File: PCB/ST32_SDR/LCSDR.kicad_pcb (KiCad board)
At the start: 2 copper layers, 150 x 95 mm, 121 parts, among them J1 MIC_PTT, J10 Conn_01x01, J11 Conn_01x01, J2 IDC10 Serial Wire, J3 Audio-Jack-3_2Switches, J4 LINEIN, J5 USB_B_Mini, J6 IQ, J7 CLK, J8 Conn_01x01, J9 Conn_01x01, K1 FRT5, K2 FRT5, Q1 Q_NPN_BEC, Q2 Q_NPN_BEC, Q7 BC817, SW1 SW_Push_Dual, SW2 SW_Push_Dual, SW3 SW_Push_Dual, SW4 SW_Push_Dual, SW5 ENCODER, SW6 SW_Push_Dual, U1 SI5351A, U15 Nokia_5110_LCD, U16 WM8731_alt, U2 FM24CL16B, U3 STM32F401RCTx, U4 AP1117-33, U5 MC34063, U6 MC34063, U7 78M09, Y1 20Mhz, Y2 Crystal

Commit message: PCB Windows 1
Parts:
- R25: moved to B.Cu
- moved R25 131.6 mm to (113.8, 66.0)
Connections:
- J2 pad 7: (no net) -> Net-(J2-Pad7)
- J2 pad 8: (no net) -> Net-(J2-Pad8)
- J3 pad 4: (no net) -> Net-(J3-Pad4)
- J3 pad 5: (no net) -> Net-(J3-Pad5)
- J5 pad 1: (no net) -> Net-(J5-Pad1)
- J5 pad 4: (no net) -> Net-(J5-Pad4)
- J6 pad 3: (no net) -> Net-(J6-Pad3)
- J6 pad 4: (no net) -> Net-(J6-Pad4)
- J6 pad 5: (no net) -> Net-(J6-Pad5)
- J6 pad 6: (no net) -> Net-(J6-Pad6)
- K2 pad 2: (no net) -> Net-(K2-Pad2)
- K2 pad 4: (no net) -> Q_OUT
- K2 pad 7: (no net) -> I_OUT
- R5 pad 2: (no net) -> TX2
- RN3 pad 5: (no net) -> Net-(RN3-Pad5)
- RN3 pad 6: (no net) -> Net-(RN3-Pad6)
- RN3 pad 7: (no net) -> Net-(RN3-Pad7)
- RN3 pad 8: (no net) -> Net-(RN3-Pad8)
- U16 pad 12: (no net) -> LINE_OUT_LEFT
- U16 pad 2: (no net) -> Net-(U16-Pad2)
- U16 pad 26: (no net) -> Net-(U16-Pad26)
- U2 pad 1: (no net) -> Net-(U2-Pad1)
- U2 pad 2: (no net) -> Net-(U2-Pad2)
- U2 pad 3: (no net) -> Net-(U2-Pad3)
- U3 pad 1: (no net) -> Net-(U3-Pad1)
- U3 pad 10: (no net) -> Net-(U3-Pad10)
- U3 pad 11: (no net) -> Net-(U3-Pad11)
- U3 pad 13: (no net) -> Net-(U3-Pad13)
- U3 pad 14: ENCODER_A -> Net-(U3-Pad14)
- U3 pad 15: ENCODER_B -> Net-(U3-Pad15)
- U3 pad 16: (no net) -> Net-(U3-Pad16)
- U3 pad 17: (no net) -> Net-(U3-Pad17)
- U3 pad 20: (no net) -> Net-(U3-Pad20)
- U3 pad 21: (no net) -> Net-(U3-Pad21)
- U3 pad 22: (no net) -> ENCODER_A
- U3 pad 23: (no net) -> ENCODER_B
- U3 pad 24: LCD_RESET -> Net-(U3-Pad24)
- U3 pad 25: LCD_LIGHT -> Net-(U3-Pad25)
- U3 pad 38: (no net) -> Net-(U3-Pad38)
- U3 pad 39: (no net) -> Net-(U3-Pad39)
- U3 pad 40: KEY_MENU -> I2C_SDA_MCU
- U3 pad 41: TX1 -> I2C_SCL_MCU
- U3 pad 42: (no net) -> Net-(U3-Pad42)
- U3 pad 43: (no net) -> Net-(U3-Pad43)
- U3 pad 54: (no net) -> LCD_RESET
- U3 pad 56: (no net) -> LCD_LIGHT
- U3 pad 57: (no net) -> I_IN_M2
- U3 pad 58: (no net) -> Q_IN_M1
- U3 pad 59: (no net) -> Q_IN_M2
- U3 pad 61: I2C_SCL_MCU -> Net-(U3-Pad61)
- U3 pad 62: I2C_SDA_MCU -> Net-(U3-Pad62)
- U3 pad 8: (no net) -> Net-(U3-Pad8)
- U3 pad 9: (no net) -> Net-(U3-Pad9)
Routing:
- net SWDIO: track 35.7 -> 44.5 mm, vias 2 -> 3
- net I2C_SCL_MCU: track 0.00 -> 8.40 mm
- net +3V3: track 18.8 -> 27.1 mm
- net Net-(R8-Pad1): track 0.00 -> 7.40 mm
- net I2C_SDA_MCU: track 0.00 -> 6.31 mm
- net ENCODER_A: track 0.00 -> 4.20 mm
- net ENCODER_B: track 0.00 -> 3.40 mm

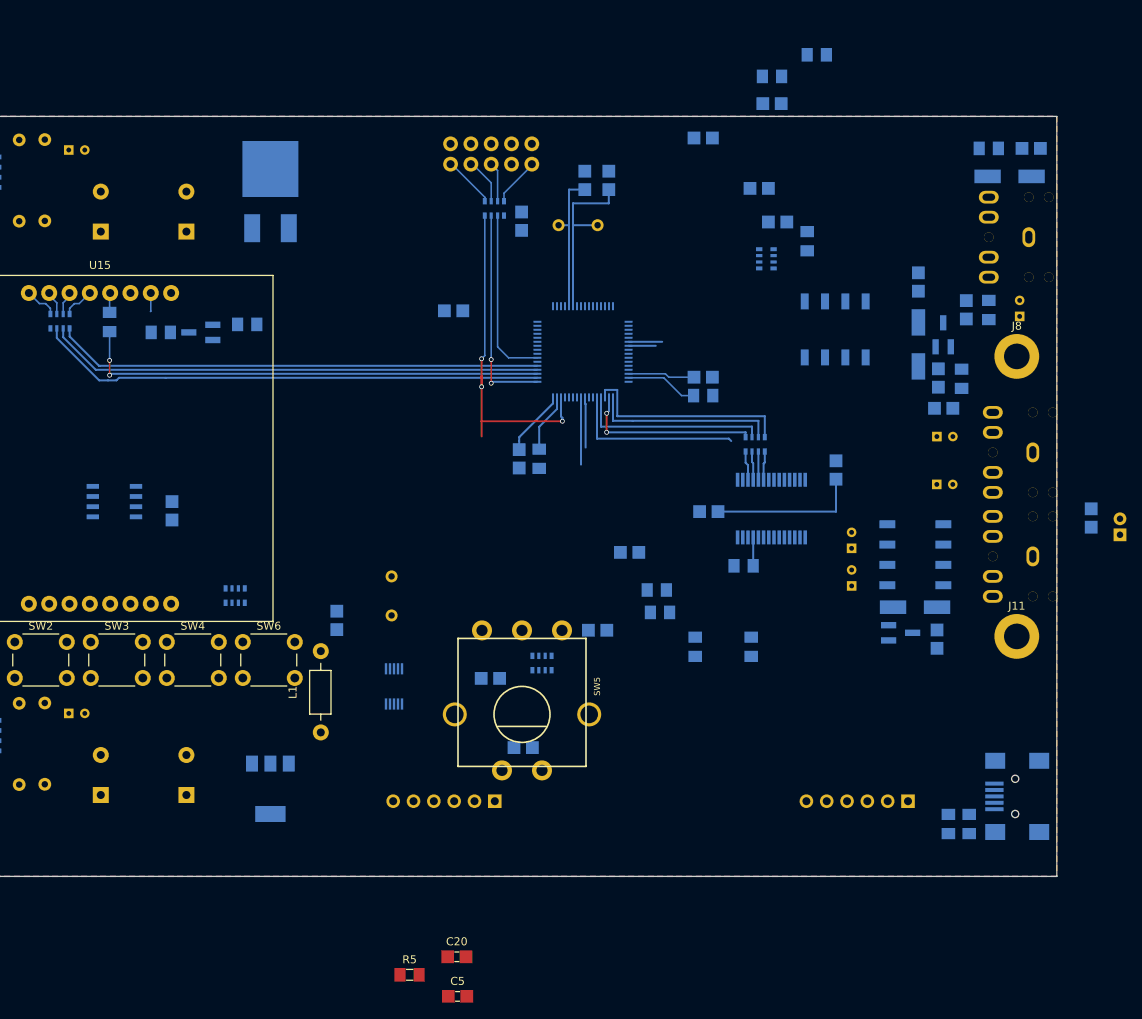
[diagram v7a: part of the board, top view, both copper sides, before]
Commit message: PCB Linux 2, update AUDIO_OUT
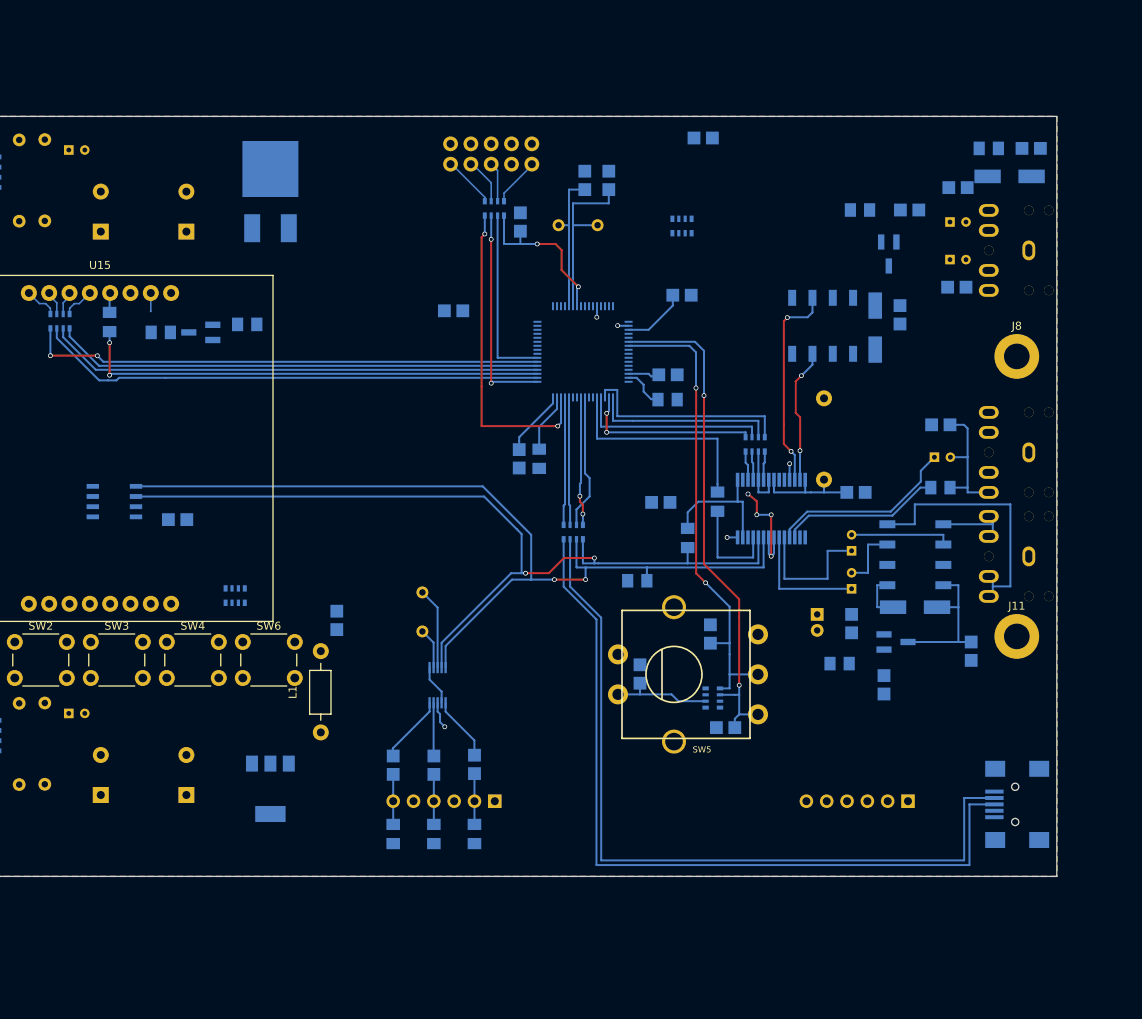
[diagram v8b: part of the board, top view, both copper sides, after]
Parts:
- removed J5: USB_B_Mini, Connect:USB_Mini-B
- removed R17, R18: 33, UI:R_1206_0603
- removed R22, R23: 56, UI:R_1206_0603
- added J12: USB_B_Mini, Connect:USB_Mini-B, B.Cu at (210.0, 126.0)
- added L4: 100uH, Choke_Axial_ThroughHole:Choke_Horizontal_RM10mm, B.Cu at (185.9, 80.4)
- added RN4: 47, Resistors_SMD:R_Array_Convex_4x0603, B.Cu at (154.6, 92.0)
- C20, C5, R5: moved to B.Cu
- moved R2 108.5 mm to (137.1, 129.7), turned to 270 degrees
- moved R3 105.9 mm to (132.1, 129.7), turned to 270 degrees
- moved C20 104.5 mm to (202.5, 61.4), turned to 180 degrees
- moved C4 95.3 mm to (132.1, 121.1), turned to 90 degrees
- moved R1 85.0 mm to (142.2, 129.7)
- moved C3 82.8 mm to (137.1, 121.1), turned to 90 degrees
- moved C2 77.7 mm to (142.2, 121.0), turned to 90 degrees
- moved R5 66.3 mm to (187.8, 108.4), turned to 180 degrees
- moved C5 66.0 mm to (193.4, 111.0), turned to 270 degrees
- moved C116 39.1 mm to (185.1, 102.2), turned to 270 degrees
- moved C33 32.8 mm to (168.2, 62.4)
- moved C44 32.7 mm to (189.3, 103.4), turned to 270 degrees
- moved C19 28.1 mm to (201.7, 57.9)
- moved C23 28.1 mm to (171.7, 104.7), turned to 90 degrees
- moved C18 27.6 mm to (202.7, 48.9)
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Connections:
- C2 pad 1: CLK0 -> CLK2
- C4 pad 1: CLK2 -> CLK0
- C45 pad 2: +3V3 -> Net-(C45-Pad2)
- J2 pad 7: Net-(J2-Pad7) -> (no net)
- J2 pad 8: Net-(J2-Pad8) -> (no net)
- J3 pad 4: Net-(J3-Pad4) -> (no net)
- J3 pad 5: Net-(J3-Pad5) -> (no net)
- J6 pad 3: Net-(J6-Pad3) -> (no net)
- J6 pad 4: Net-(J6-Pad4) -> (no net)
- J6 pad 5: Net-(J6-Pad5) -> (no net)
- J6 pad 6: Net-(J6-Pad6) -> (no net)
- J7 pad 2: CLK0 -> CLK2
- J7 pad 6: CLK2 -> CLK0
- K2 pad 2: Net-(K2-Pad2) -> (no net)
- K2 pad 4: Q_OUT -> (no net)
- K2 pad 7: I_OUT -> (no net)
- R1 pad 1: CLK0 -> CLK2
- R3 pad 1: CLK2 -> CLK0
- RN3 pad 5: Net-(RN3-Pad5) -> (no net)
- RN3 pad 6: Net-(RN3-Pad6) -> (no net)
- RN3 pad 7: Net-(RN3-Pad7) -> (no net)
- RN3 pad 8: Net-(RN3-Pad8) -> (no net)
- RN9 pad 1: KEY_MENU -> ENCODER_B
- RN9 pad 2: ENCODER_B -> ENCODER_A
- RN9 pad 3: ENCODER_A -> +3V3
- RN9 pad 4: KEY_E -> (no net)
- RN9 pad 5: +3V3 -> KEY_E
- RN9 pad 6: +3V3 -> KEY_MENU
- U1 pad 10: Net-(C2-Pad2) -> Net-(C4-Pad2)
- U1 pad 6: Net-(C4-Pad2) -> Net-(C2-Pad2)
- U16 pad 14: +3V3 -> Net-(C45-Pad2)
- U16 pad 2: Net-(U16-Pad2) -> (no net)
- U16 pad 26: Net-(U16-Pad26) -> (no net)
- U16 pad 8: +3V3 -> Net-(C45-Pad2)
- U2 pad 1: Net-(U2-Pad1) -> (no net)
- U2 pad 2: Net-(U2-Pad2) -> (no net)
- U2 pad 3: Net-(U2-Pad3) -> (no net)
- U3 pad 1: Net-(U3-Pad1) -> (no net)
- U3 pad 10: Net-(U3-Pad10) -> BAND2
- U3 pad 11: Net-(U3-Pad11) -> BAND3
- U3 pad 13: Net-(U3-Pad13) -> (no net)
- U3 pad 14: Net-(U3-Pad14) -> (no net)
- U3 pad 15: Net-(U3-Pad15) -> (no net)
- U3 pad 16: Net-(U3-Pad16) -> (no net)
- U3 pad 17: Net-(U3-Pad17) -> (no net)
- U3 pad 20: Net-(U3-Pad20) -> (no net)
- U3 pad 21: Net-(U3-Pad21) -> TX1
- U3 pad 24: Net-(U3-Pad24) -> (no net)
- U3 pad 25: Net-(U3-Pad25) -> (no net)
- U3 pad 26: BAND0 -> (no net)
- U3 pad 27: BAND1 -> (no net)
- U3 pad 28: BAND2 -> (no net)
- U3 pad 29: BAND3 -> (no net)
- U3 pad 38: Net-(U3-Pad38) -> (no net)
- U3 pad 39: Net-(U3-Pad39) -> TX2
- U3 pad 42: Net-(U3-Pad42) -> (no net)
- U3 pad 43: Net-(U3-Pad43) -> (no net)
- U3 pad 57: I_IN_M2 -> (no net)
- U3 pad 58: Q_IN_M1 -> (no net)
- U3 pad 59: Q_IN_M2 -> (no net)
- U3 pad 61: Net-(U3-Pad61) -> (no net)
- U3 pad 62: Net-(U3-Pad62) -> (no net)
- U3 pad 8: Net-(U3-Pad8) -> BAND0
- U3 pad 9: Net-(U3-Pad9) -> BAND1
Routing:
- net I2C_SDA: track 0.00 -> 115.0 mm, vias 0 -> 2
- net I2C_SCL: track 0.00 -> 112.5 mm, vias 0 -> 2
- net Net-(J12-Pad3): track 0.00 -> 99.7 mm
- net Net-(J12-Pad2): track 0.00 -> 98.7 mm
- net LCD_RESET: track 0.00 -> 64.6 mm, vias 0 -> 2
- net ENCODER_A: track 4.20 -> 63.8 mm, vias 0 -> 2
- net ENCODER_B: track 3.40 -> 59.7 mm, vias 0 -> 2
- net Net-(J4-Pad1): track 0.00 -> 32.8 mm
- net LINE_OUT_LEFT: track 0.00 -> 26.3 mm, vias 0 -> 2
- net GND: track 0.00 -> 24.6 mm, vias 0 -> 9
- net MIC_IN: track 0.00 -> 23.6 mm
- net MCU_RESET: track 0.00 -> 20.6 mm, vias 0 -> 2
- net MIC_BIAS: track 0.00 -> 20.1 mm
- net Net-(C16-Pad1): track 0.00 -> 20.0 mm
- net Net-(C49-Pad2): track 0.00 -> 17.7 mm
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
